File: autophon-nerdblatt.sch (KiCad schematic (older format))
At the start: 4 parts, among them J1 board-edge-connector, U2 L298HN, U3 L298HN, U4 L298HN

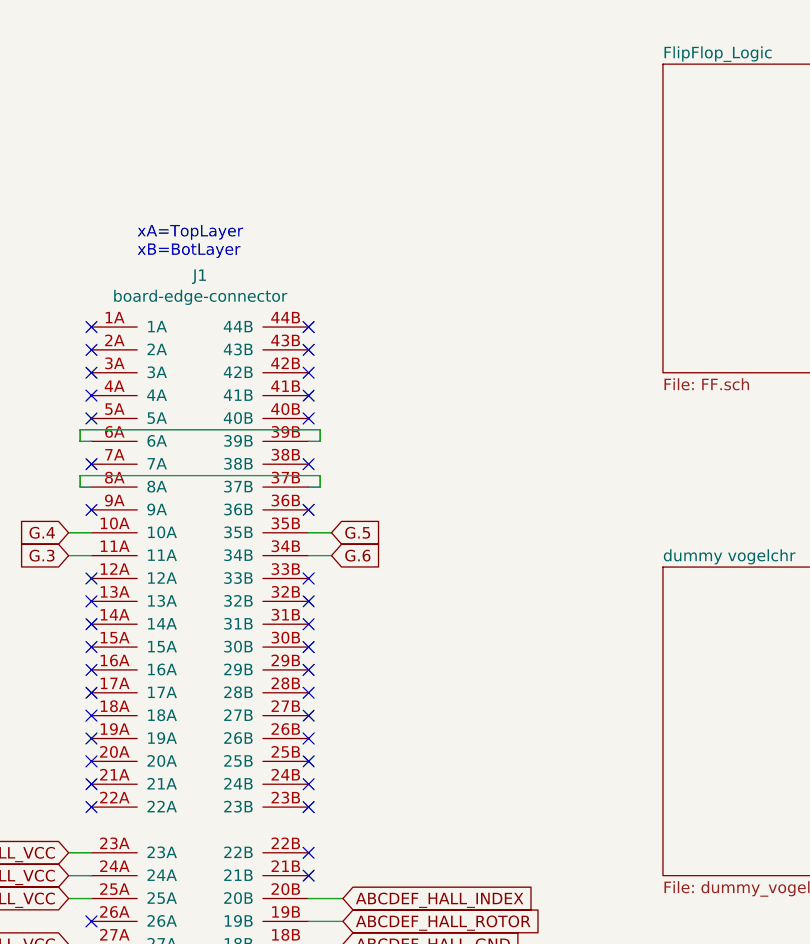
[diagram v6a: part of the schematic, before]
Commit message: Minor cleanup, adding the w1_test_pcb_lib, just for the single gate buffer.
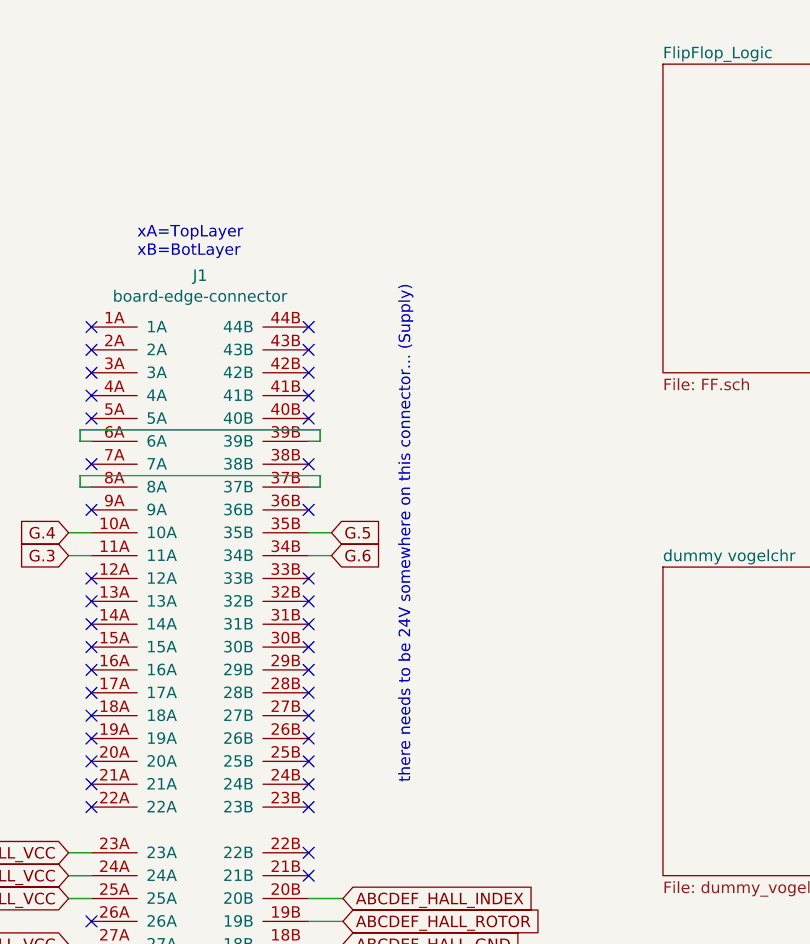
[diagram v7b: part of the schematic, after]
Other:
- note added: "there needs to be 24V somewhere on this connector... (Supply)"
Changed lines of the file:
@@
 F1 "dummy_vogelchr.sch" 50
 $EndSheet
+Text Notes 4850 3900 1    50   ~ 0
+there needs to be 24V somewhere on this connector... (Supply)
 $EndSCHEMATC

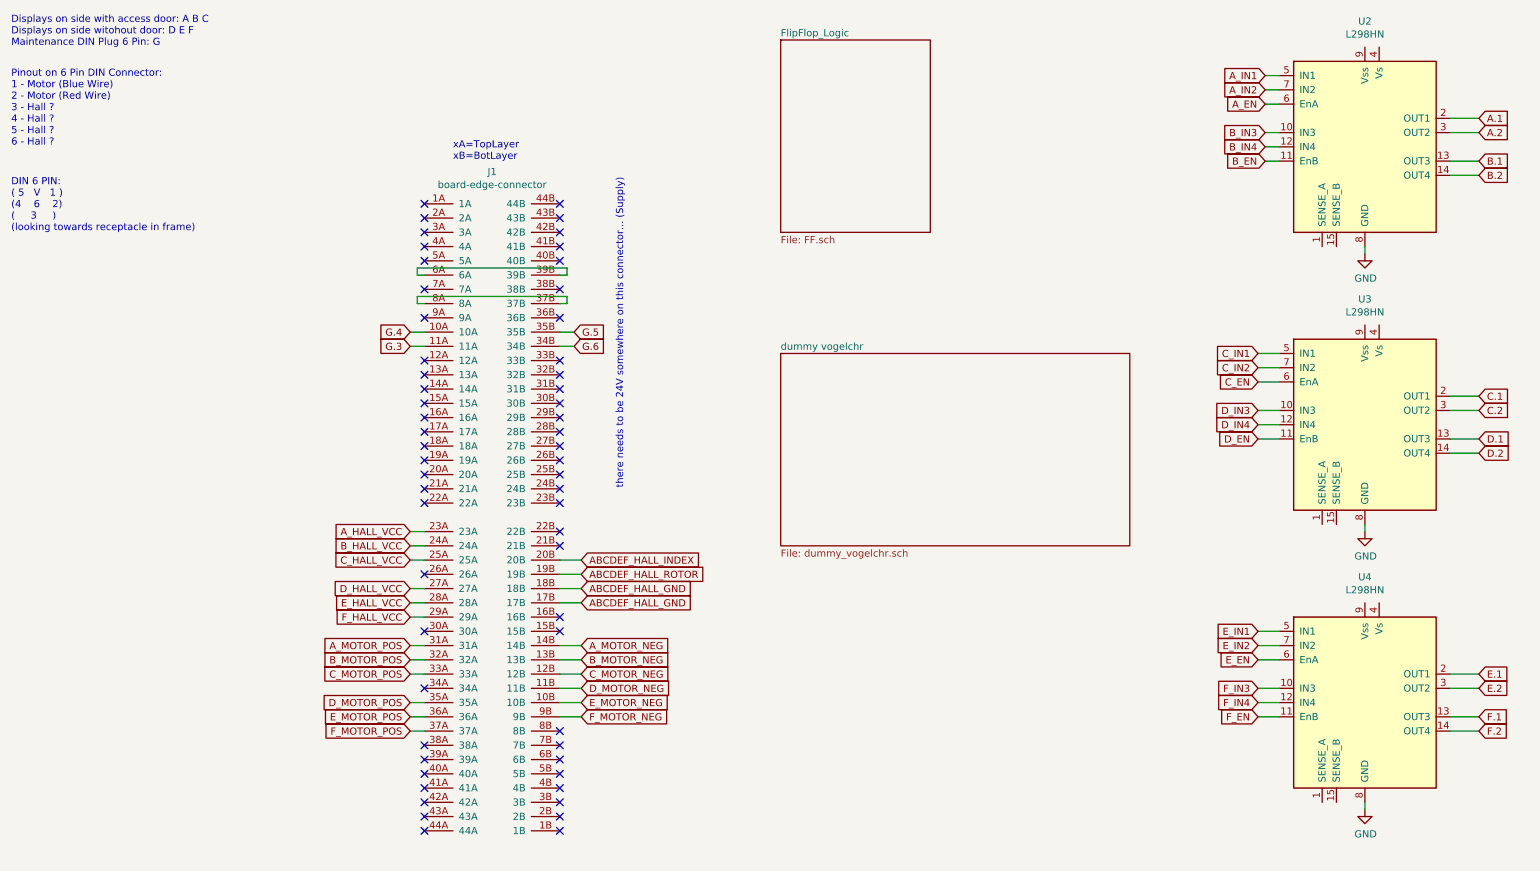
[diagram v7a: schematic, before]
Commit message: Remove FF and "dummy" .sch, add voltage regulators.
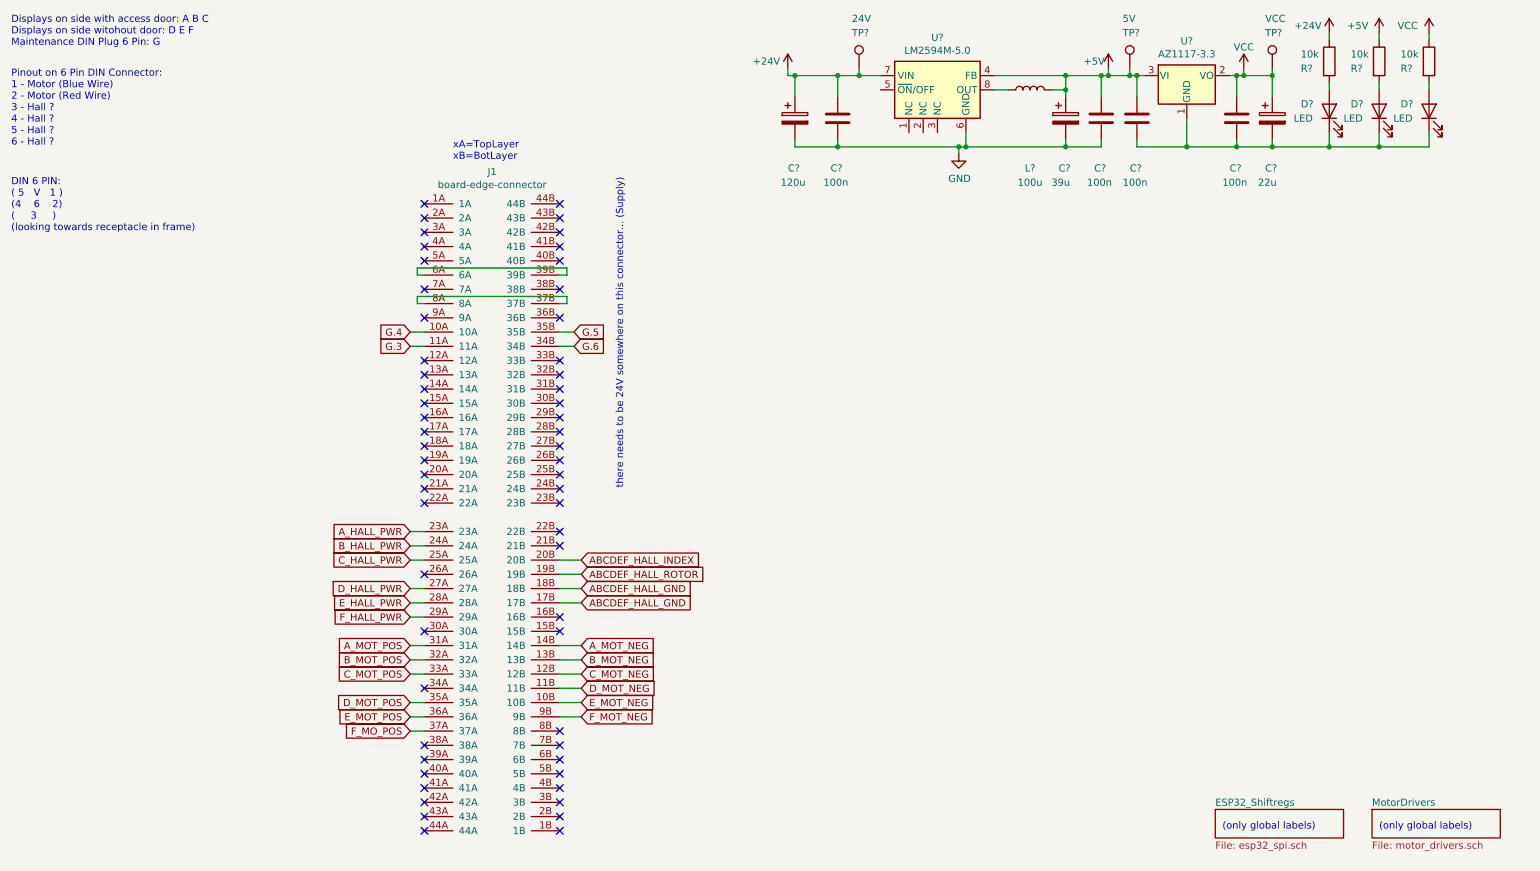
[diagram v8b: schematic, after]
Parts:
- removed U2, U3, U4: L298HN, Package_TO_SOT_THT:TO-220F-15_P2.54x5.08mm_StaggerOdd_Lead5.08mm_Vertical, symbol Driver_Motor:L298HN
- added C? (x4): 100n, symbol Device:C
- added C?: 120u, symbol Device:CP
- added C?: 39u, symbol Device:CP
- added C?: 22u, symbol Device:CP
- added D? (x3): LED, symbol Device:LED
- added L?: 100u, symbol Device:L
- added R? (x3): 10k, symbol Device:R
- added TP?: VCC, symbol Connector:TestPoint
- added TP?: 5V, symbol Connector:TestPoint
- added TP?: 24V, symbol Connector:TestPoint
- added U?: LM2594M-5.0, Package_SO:SOIC-8_3.9x4.9mm_P1.27mm, symbol Regulator_Switching:LM2594M-5.0
- added U?: AZ1117-3.3, symbol Regulator_Linear:AZ1117-3.3
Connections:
- net GND: now also C?.2, C?.2, C?.2, C?.2, U?.6 (GND)
- net A_HALL_VCC renamed A_HALL_PWR
- net A_MOTOR_NEG renamed A_MOT_NEG
- net A_MOTOR_POS renamed A_MOT_POS
- net B_HALL_VCC renamed B_HALL_PWR
- net B_MOTOR_NEG renamed B_MOT_NEG
- net B_MOTOR_POS renamed B_MOT_POS
- net C_HALL_VCC renamed C_HALL_PWR
- net C_MOTOR_NEG renamed C_MOT_NEG
- net C_MOTOR_POS renamed C_MOT_POS
- net D_HALL_VCC renamed D_HALL_PWR
- net D_MOTOR_NEG renamed D_MOT_NEG
- net D_MOTOR_POS renamed D_MOT_POS
- net E_HALL_VCC renamed E_HALL_PWR
- net E_MOTOR_NEG renamed E_MOT_NEG
- net E_MOTOR_POS renamed E_MOT_POS
- net F_HALL_VCC renamed F_HALL_PWR
- net F_MOTOR_NEG renamed F_MOT_NEG
- net F_MOTOR_POS renamed F_MO_POS
- new net: L?.1, U?.8 (OUT)
- new net: C?.2, C?.2, C?.2, D?.1 (K), D?.1 (K), D?.1 (K), U?.1 (GND)
- new net: D?.2 (A), R?.2 (x3)
- new net +24V: C?.1, C?.1, R?.1, TP?.1, U?.7 (VIN)
- new net +5V: C?.1, C?.1, C?.1, L?.2, R?.1, TP?.1, U?.3 (VI), U?.4 (FB)
- new net VCC: C?.1, C?.1, R?.1, TP?.1, U?.2 (VO)
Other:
- note added: "(only global labels)"
